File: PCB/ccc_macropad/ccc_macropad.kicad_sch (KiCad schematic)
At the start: 18 parts, among them SW1 SW_Push, SW2 SW_Push, SW3 OS/Left_Right-hand_Switch, SW4 SW_Push, SW5 SW_Push, U2 XIAO-RP2040-DIP

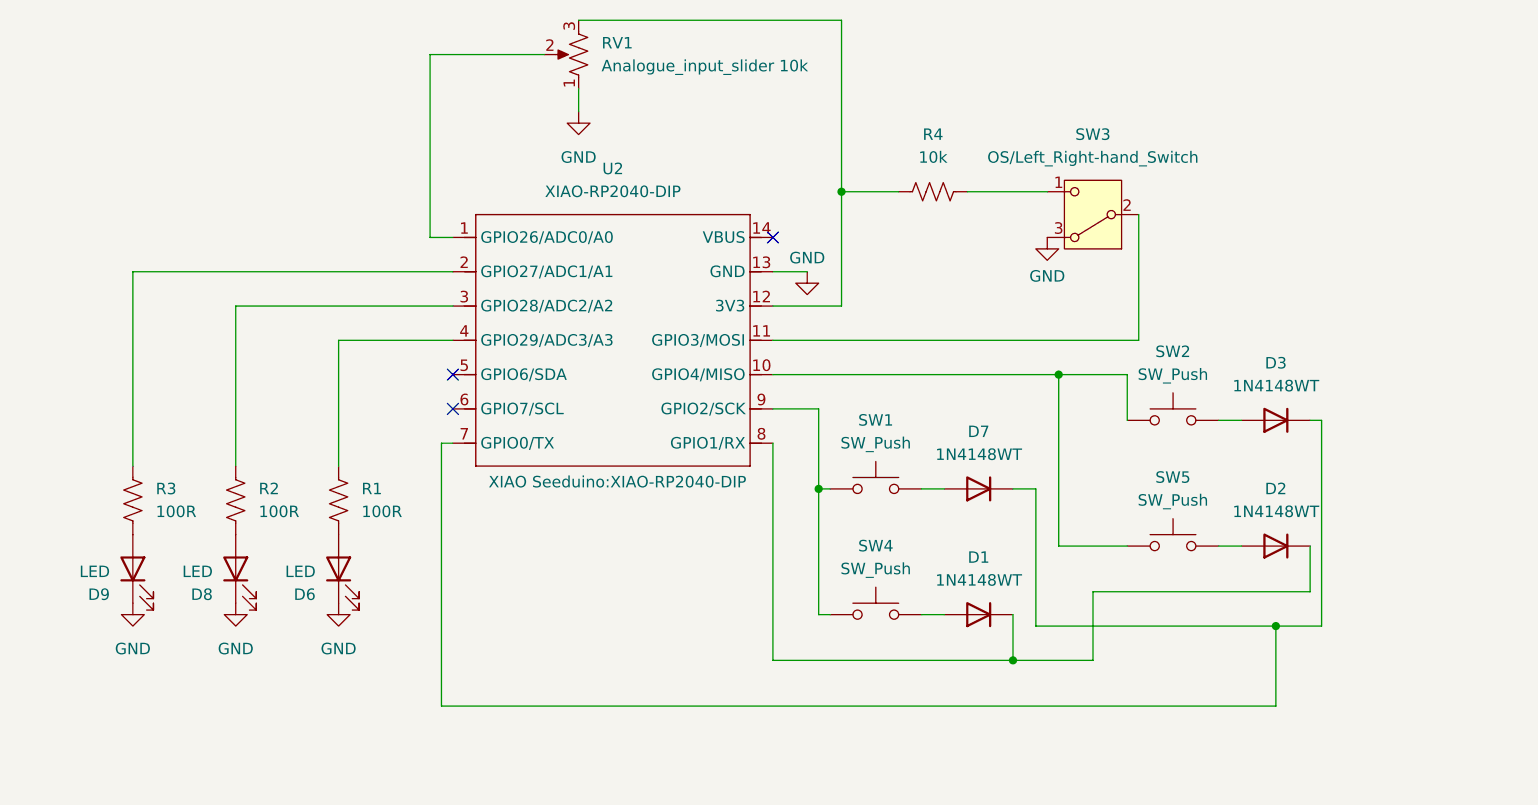
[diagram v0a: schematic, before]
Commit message: feat: update schematic to rp2040_zero
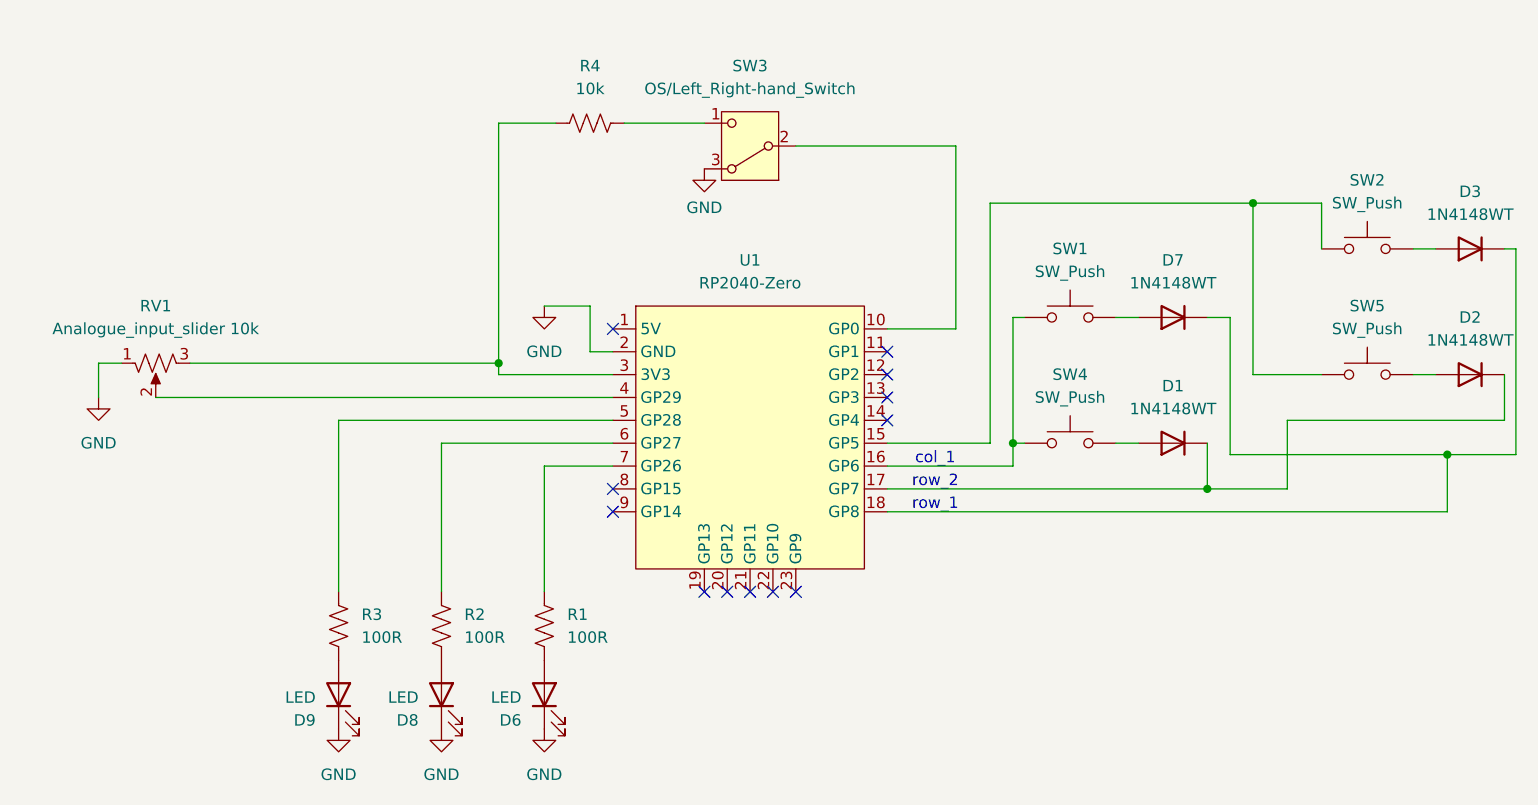
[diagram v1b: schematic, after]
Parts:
- removed U2: XIAO-RP2040-DIP, XIAO Seeduino:XIAO-RP2040-DIP, symbol Seeed XIAO:XIAO-RP2040-DIP
- added U1: RP2040-Zero, CustomFootprints:RP2040 Zero, symbol rp2040_zero:RP2040-Zero
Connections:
- net GND: now also U1.2 (GND)
- net at R4.2, RV1.3: now also U1.3 (3V3)
- net at SW1.1, SW4.1: now also U1.16 (GP6)
- net at RV1.2: now also U1.4 (GP29)
- net at SW2.1, SW5.1: now also U1.15 (GP5)
- net at SW3.2 (B): now also U1.10 (GP0)
- net at R3.2: now also U1.5 (GP28)
- net at R2.2: now also U1.6 (GP27)
- net at R1.2: now also U1.7 (GP26)
- net at D3.1 (K), D7.1 (K): now also U1.18 (GP8)
- net at D1.1 (K), D2.1 (K): now also U1.17 (GP7)
- no-connect marks 3 -> 12
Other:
- note added: "col_1"
- note added: "row_1"
- note added: "row_2"
- moved on the sheet: D1, D2, D3, D6, D7, D8, D9, R1, R2, R3, R4, RV1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

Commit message: PCB: feat add pinout table
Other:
- note added: "GPIO placement"
- note removed: "row_1"
- moved on the sheet: RV1

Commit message: PCB:chores: cleanup schematic
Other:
- note removed: "col_1"
- note removed: "row_2"
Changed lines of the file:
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@@
-		)
-	)
-	(text "row_2"
-		(exclude_from_sim no)
-		(at 167.894 112.268 0)
-		(effects
-			(font
-				(size 1.27 1.27)
-			)
-		)
-	)
-	(text "col_1"
-		(exclude_from_sim no)
-		(at 167.894 109.728 0)
-		(effects
-			(font
-				(size 1.27 1.27)
-			)
 		)
 	)

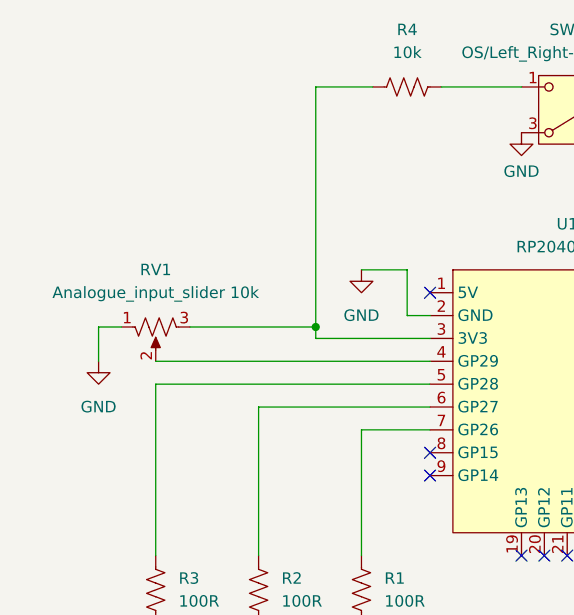
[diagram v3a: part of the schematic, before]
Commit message: feat: add buffer capacitor//increase board size// add foot holes
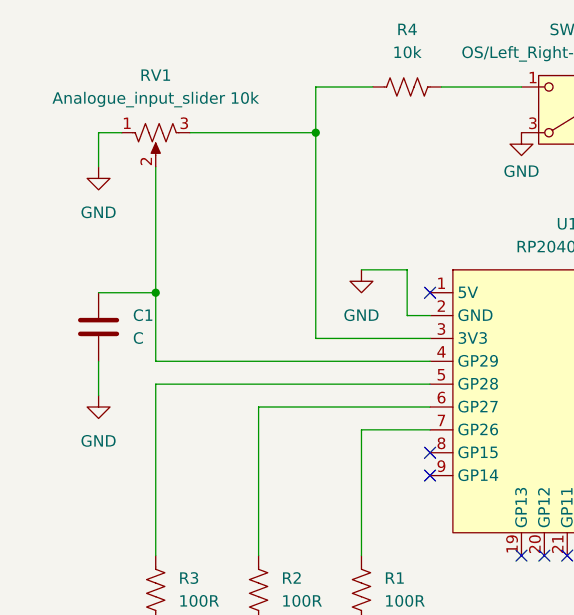
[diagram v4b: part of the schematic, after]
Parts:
- added C1: C, Capacitor_THT:C_Disc_D5.0mm_W2.5mm_P5.00mm, symbol Device:C
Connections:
- net GND: now also C1.2
- net at RV1.2, U1.4 (GP29): now also C1.1
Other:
- moved on the sheet: RV1
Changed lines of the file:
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@@
 	)
 	(junction
-		(at 119.38 99.06)
+		(at 101.6 95.25)
 		(diameter 0)
 		(color 0 0 0 0)
 	)
+	(junction
+		(at 119.38 77.47)
+		(diameter 0)
+		(color 0 0 0 0)
+	)
 	(no_connect
 		(at 149.86 124.46)
@@
 	(wire
 		(pts
-			(xy 105.41 99.06) (xy 119.38 99.06)
+			(xy 95.25 102.87) (xy 95.25 106.68)
+		)
+		(stroke
+			(width 0)
+			(type default)
+		)
+	)
+	(wire
+		(pts
+			(xy 105.41 77.47) (xy 119.38 77.47)
 		)
 		(stroke
@@
 	(wire
 		(pts
-			(xy 95.25 99.06) (xy 97.79 99.06)
+			(xy 95.25 77.47) (xy 97.79 77.47)
 		)
 		(stroke
@@
 	(wire
 		(pts
-			(xy 119.38 72.39) (xy 119.38 99.06)
+			(xy 119.38 72.39) (xy 119.38 77.47)
 		)
 		(stroke
@@
 	(wire
 		(pts
-			(xy 95.25 102.87) (xy 95.25 99.06)
+			(xy 95.25 81.28) (xy 95.25 77.47)
 		)
 		(stroke
@@
 	(wire
 		(pts
+			(xy 203.2 81.28) (xy 210.82 81.28)
+		)
+		(stroke
+			(width 0)
+			(type default)
+		)
+	)
+	(wire
+		(pts
+			(xy 176.53 107.95) (xy 176.53 93.98)
+		)
+		(stroke
+			(width 0)
+			(type default)
+		)
+	)
+	(wire
+		(pts
+			(xy 173.99 81.28) (xy 203.2 81.28)
+		)
+		(stroke
+			(width 0)
+			(type default)
+		)
+	)
+	(wire
+		(pts
+			(xy 203.2 81.28) (xy 203.2 100.33)
+		)
+		(stroke
+			(width 0)
+			(type default)
+		)
+	)
+	(wire
+		(pts
+			(xy 101.6 95.25) (xy 101.6 102.87)
+		)
+		(stroke
+			(width 0)
+			(type default)
+		)
+	)
+	(wire
+		(pts
+			(xy 152.4 74.93) (xy 170.18 74.93)
+		)
+		(stroke
+			(width 0)
+			(type default)
+		)
+	)
+	(wire
+		(pts
+			(xy 119.38 77.47) (xy 119.38 100.33)
+		)
+		(stroke
+			(width 0)
+			(type default)
+		)
+	)
+	(wire
+		(pts
+			(xy 232.41 109.22) (xy 232.41 86.36)
+		)
+		(stroke
+			(width 0)
+			(type default)
+		)
+	)
+	(wire
+		(pts
 			(xy 101.6 102.87) (xy 132.08 102.87)
 		)
@@
 	(wire
 		(pts
-			(xy 203.2 81.28) (xy 210.82 81.28)
-		)
-		(stroke
-			(width 0)
-			(type default)
-		)
-	)
-	(wire
-		(pts
-			(xy 176.53 107.95) (xy 176.53 93.98)
-		)
-		(stroke
-			(width 0)
-			(type default)
-		)
-	)
-	(wire
-		(pts
-			(xy 173.99 81.28) (xy 203.2 81.28)
-		)
-		(stroke
-			(width 0)
-			(type default)
-		)
-	)
-	(wire
-		(pts
-			(xy 203.2 81.28) (xy 203.2 100.33)
-		)
-		(stroke
-			(width 0)
-			(type default)
-		)
-	)
-	(wire
-		(pts
-			(xy 152.4 74.93) (xy 170.18 74.93)
-		)
-		(stroke
-			(width 0)
-			(type default)
-		)
-	)
-	(wire
-		(pts
-			(xy 232.41 109.22) (xy 232.41 86.36)
-		)
-		(stroke
-			(width 0)
-			(type default)
-		)
-	)
-	(wire
-		(pts
 			(xy 124.46 110.49) (xy 132.08 110.49)
 		)
@@
 	(wire
 		(pts
+			(xy 95.25 95.25) (xy 101.6 95.25)
+		)
+		(stroke
+			(width 0)
+			(type default)
+		)
+	)
+	(wire
+		(pts
 			(xy 207.01 113.03) (xy 207.01 105.41)
 		)
@@
 	(wire
 		(pts
-			(xy 119.38 99.06) (xy 119.38 100.33)
-		)
-		(stroke
-			(width 0)
-			(type default)
-		)
-	)
-	(wire
-		(pts
 			(xy 190.5 107.95) (xy 187.96 107.95)
 		)
@@
 		(pts
 			(xy 129.54 92.71) (xy 124.46 92.71)
+		)
+		(stroke
+			(width 0)
+			(type default)
+		)
+	)
+	(wire
+		(pts
+			(xy 101.6 81.28) (xy 101.6 95.25)
 		)
 		(stroke
@@
 	(symbol
 		(lib_id "Device:R_Potentiometer_US")
-		(at 101.6 99.06 90)
+		(at 101.6 77.47 90)
 		(mirror x)
 		(unit 1)
@@
 		(dnp no)
 		(property "Reference" "RV1"
-			(at 101.6 92.71 90)
+			(at 101.6 71.12 90)
 			(effects
 				(font
@@
 		)
 		(property "Value" "Analogue_input_slider 10k"
-			(at 101.6 95.25 90)
+			(at 101.6 73.66 90)
 			(effects
 				(font
@@
 		)
 		(property "Footprint" "CustomFootprints:Potentiometer_slide_75mm_range_60mm_2_sets"
-			(at 101.6 99.06 0)
+			(at 101.6 77.47 0)
 			(effects
 				(font
@@
 		)
 		(property "Datasheet" "~"
-			(at 101.6 99.06 0)
+			(at 101.6 77.47 0)
 			(effects
 				(font
@@
 		)
 		(property "Description" "Potentiometer, US symbol"
-			(at 101.6 99.06 0)
+			(at 101.6 77.47 0)
 			(effects
 				(font
@@
 	(symbol
 		(lib_id "power:GND")
-		(at 95.25 102.87 0)
+		(at 95.25 106.68 0)
+		(unit 1)
+		(exclude_from_sim no)
+		(in_bom yes)
+		(on_board yes)
+		(dnp no)
+		(fields_autoplaced yes)
+		(property "Reference" "#PWR03"
+			(at 95.25 113.03 0)
+			(effects
+				(font
+					(size 1.27 1.27)
+				)
+				(hide yes)
+			)
+		)
+		(property "Value" "GND"
+			(at 95.25 111.76 0)
+			(effects
+				(font
+					(size 1.27 1.27)
+				)
+			)
+		)
+		(property "Footprint" ""
+			(at 95.25 106.68 0)
+			(effects
+				(font
+					(size 1.27 1.27)
+				)
+				(hide yes)
+			)
+		)
+		(property "Datasheet" ""
+			(at 95.25 106.68 0)
+			(effects
+				(font
+					(size 1.27 1.27)
+				)
+				(hide yes)
+			)
+		)
+		(property "Description" "Power symbol creates a global label with name \"GND\" , ground"
+			(at 95.25 106.68 0)
+			(effects
+				(font
+					(size 1.27 1.27)
+				)
+				(hide yes)
+			)
+		)
+		(pin "1"
+		)
+		(instances
+			(project "ccc_macropad"
+				(path "/30b7c58f-86a9-47fb-ba55-c2e4c0b4123f"
+					(reference "#PWR03")
+					(unit 1)
+				)
+			)
+		)
+	)
+	(symbol
+		(lib_id "power:GND")
+		(at 95.25 81.28 0)
 		(unit 1)
 		(exclude_from_sim no)
@@
 		(fields_autoplaced yes)
 		(property "Reference" "#PWR02"
-			(at 95.25 109.22 0)
+			(at 95.25 87.63 0)
 			(effects
 				(font
@@
 		)
 		(property "Value" "GND"
-			(at 95.25 107.95 0)
+			(at 95.25 86.36 0)
 			(effects
 				(font
@@
 		)
 		(property "Footprint" ""
-			(at 95.25 102.87 0)
+			(at 95.25 81.28 0)
 			(effects
 				(font
@@
 		)
 		(property "Datasheet" ""
-			(at 95.25 102.87 0)
+			(at 95.25 81.28 0)
 			(effects
 				(font
@@
 		)
 		(property "Description" "Power symbol creates a global label with name \"GND\" , ground"
-			(at 95.25 102.87 0)
+			(at 95.25 81.28 0)
 			(effects
 				(font
@@
 					(unit 1)
 				)
+			)
+		)
+	)
+	(symbol
+		(lib_id "Device:C")
+		(at 95.25 99.06 0)
+		(unit 1)
+		(exclude_from_sim no)
+		(in_bom yes)
+		(on_board yes)
+		(dnp no)
+		(fields_autoplaced yes)
+		(property "Reference" "C1"
+			(at 99.06 97.7899 0)
+			(effects
+				(font
+					(size 1.27 1.27)
+				)
+				(justify left)
+			)
+		)
+		(property "Value" "C"
+			(at 99.06 100.3299 0)
+			(effects
+				(font
+					(size 1.27 1.27)
+				)
+				(justify left)
+			)
+		)
+		(property "Footprint" "Capacitor_THT:C_Disc_D5.0mm_W2.5mm_P5.00mm"
+			(at 96.2152 102.87 0)
+			(effects
+				(font
+					(size 1.27 1.27)
+				)
+				(hide yes)
+			)
+		)
+		(property "Datasheet" "~"
+			(at 95.25 99.06 0)
+			(effects
+				(font
+					(size 1.27 1.27)
+				)
+				(hide yes)
+			)
+		)
+		(property "Description" "Unpolarized capacitor"
+			(at 95.25 99.06 0)
+			(effects
+				(font
+					(size 1.27 1.27)
+				)
+				(hide yes)
+			)
+		)
+		(pin "1"
+		)
+		(pin "2"
+		)
+		(instances
+			(project ""
+				(path "/30b7c58f-86a9-47fb-ba55-c2e4c0b4123f"
+					(reference "C1")
+					(unit 1)
+				)
